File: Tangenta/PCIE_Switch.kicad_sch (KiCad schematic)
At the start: 0 parts

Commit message: PCIe current progress, hierarchy
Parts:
- added C1: 10uF, Capacitor_SMD:C_0402_1005Metric, symbol Device:C_Small
- added U15: PI7C9X2G404SLBFDEX, PCIE_Switch:PCIE_Switch, symbol PCIE_Switch:PI7C9X2G404SLBFDEX
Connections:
- new net 3V3: C1.1
- new net 3V3_STANDBY: C1.2
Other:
- note added: "Used for test purposes only!!!"

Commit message: PCIe current progress.
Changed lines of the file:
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@@
+    (stroke (width 0) (type default))
+  )
+  (wire (pts (xy 56.515 29.21) (xy 33.655 29.21))
     (stroke (width 0) (type default))
   )
@@
     (stroke (width 0) (type default))
   )
-  (wire (pts (xy 56.515 24.13) (xy 33.655 24.13))
+  (wire (pts (xy 56.515 19.05) (xy 33.655 19.05))
     (stroke (width 0) (type default))
   )
-  (wire (pts (xy 56.515 29.21) (xy 33.655 29.21))
+  (wire (pts (xy 56.515 24.13) (xy 33.655 24.13))
     (stroke (width 0) (type default))
   )
@@
   (text "Used for test purposes only!!!" (at 251.4601 72.3901 0)
     (effects (font (size 3 3)) (justify left bottom))
+  )
+  (label "1V0SB" (at 56.515 29.21 180) (fields_autoplaced)
+    (effects (font (size 1.27 1.27)) (justify right bottom))
   )
   (label "3V3" (at 280.6701 95.2501 0) (fields_autoplaced)
@@
     (effects (font (size 1.27 1.27)) (justify left bottom))
   )
-  (label "3V3" (at 56.515 29.21 180) (fields_autoplaced)
+  (label "3V3" (at 56.515 24.13 180) (fields_autoplaced)
     (effects (font (size 1.27 1.27)) (justify right bottom))
   )
@@
     (effects (font (size 1.27 1.27)) (justify right bottom))
   )
-  (label "3V3SB" (at 56.515 24.13 180) (fields_autoplaced)
+  (label "3V3SB" (at 56.515 19.05 180) (fields_autoplaced)
     (effects (font (size 1.27 1.27)) (justify right bottom))
   )
@@
     (effects (font (size 1.27 1.27)) (justify right))
   )
+  (hierarchical_label "1V0_STANDBY" (shape input) (at 33.655 29.21 180) (fields_autoplaced)
+    (effects (font (size 1.27 1.27)) (justify right))
+  )
   (hierarchical_label "PCIE_SW_SMBCLK" (shape input) (at 33.655 81.915 180) (fields_autoplaced)
     (effects (font (size 1.27 1.27)) (justify right))
@@
     (effects (font (size 1.27 1.27)) (justify right))
   )
-  (hierarchical_label "3V3_STANDBY" (shape input) (at 33.655 24.13 180) (fields_autoplaced)
+  (hierarchical_label "3V3_STANDBY" (shape input) (at 33.655 19.05 180) (fields_autoplaced)
     (effects (font (size 1.27 1.27)) (justify right))
   )
@@
     (effects (font (size 1.27 1.27)) (justify right))
   )
-  (hierarchical_label "3V3" (shape input) (at 33.655 29.21 180) (fields_autoplaced)
+  (hierarchical_label "3V3" (shape input) (at 33.655 24.13 180) (fields_autoplaced)
     (effects (font (size 1.27 1.27)) (justify right))
   )

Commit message: PCIe EEPROM
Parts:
- added C1: 10uF, Capacitor_SMD:C_0402_1005Metric, symbol Device:C_Small
- added C1: 100nF, Capacitor_SMD:C_0402_1005Metric, symbol Device:C_Small
- added R2 (x2): 5.1k, Resistor_SMD:R_0402_1005Metric, symbol Device:R_Small_US
- added U17: M24C04-RMN6TP, M24C04-RMN6TP:M24C04-RMN6TP, symbol M24C04-RMN6TP:M24C04-RMN6TP
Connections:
- net 3V3: now also C1.2, C1.2, R2.2, R2.2, U17.8 (VCC); no longer C1.1
- net 3V3_STANDBY: no longer C1.2
- net GNDREF: now also C1.1, C1.1, U17.2 (E1), U17.3 (E2), U17.4 (VSS), U17.7 (WC#)
- new net EE_I2C_SCL: R2.1, U17.6 (SCL)
- new net EE_I2C_SDA: R2.1, U17.5 (SDA)
- no-connect marks 0 -> 1
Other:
- note added: "EEPROM"
- note removed: "Used for test purposes only!!!"

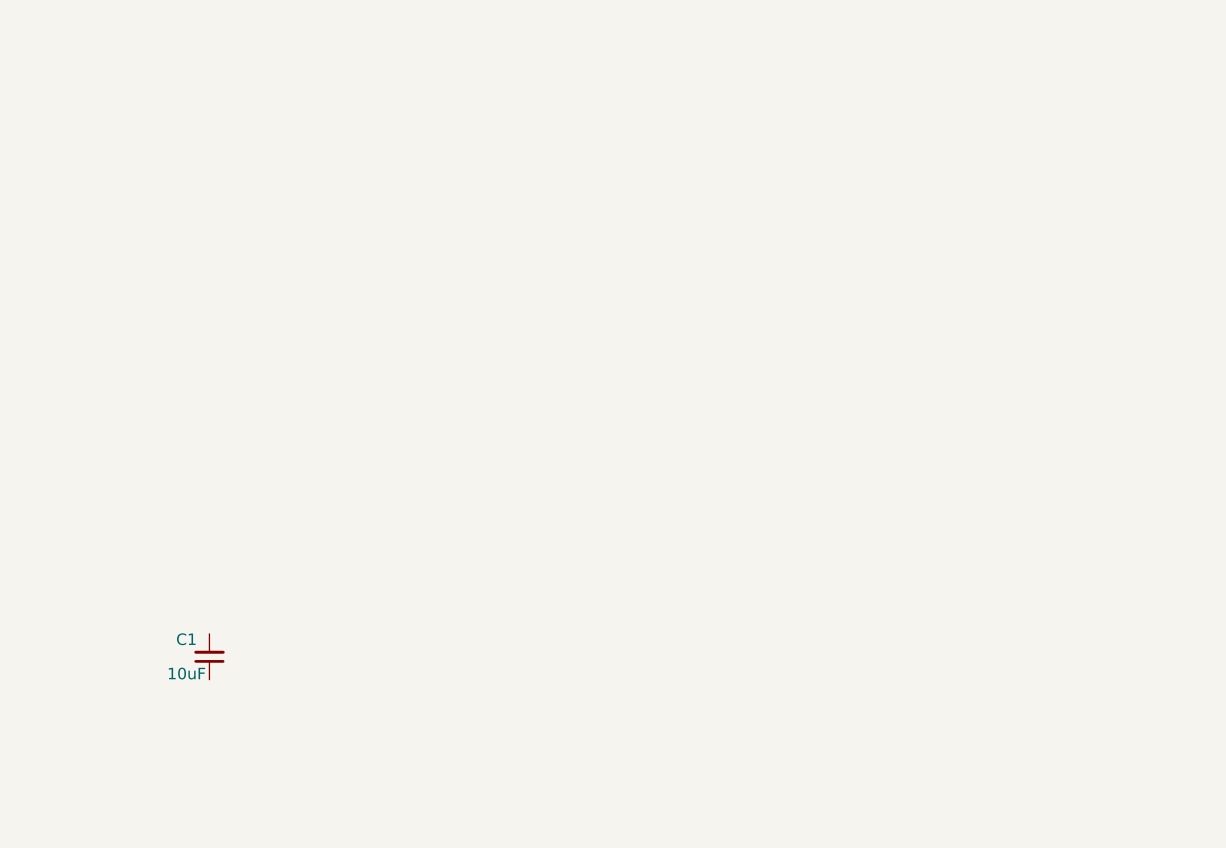
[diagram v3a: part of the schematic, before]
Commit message: PCIe 3.3V decaps.
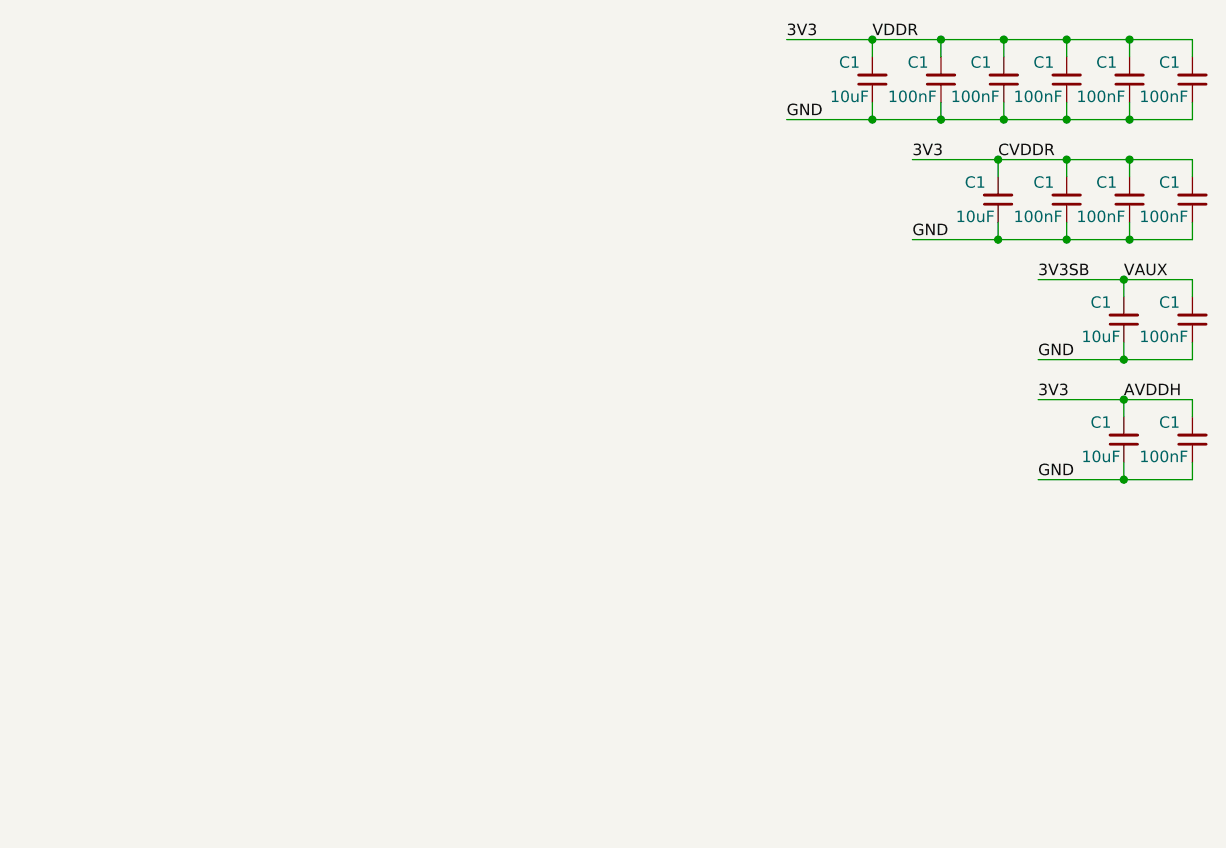
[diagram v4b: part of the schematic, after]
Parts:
- added C1 (x3): 10uF, Capacitor_SMD:C_0402_1005Metric, symbol Device:C_Small
- added C1 (x10): 100nF, Capacitor_SMD:C_0402_1005Metric, symbol Device:C_Small
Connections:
- net 3V3: now also C1.2, C1.2, C1.2, C1.2, C1.2, C1.2, C1.2, C1.2, C1.2, C1.2, C1.2, C1.2
- net 3V3_STANDBY: now also C1.2, C1.2
- net GNDREF: now also C1.1, C1.1, C1.1, C1.1, C1.1, C1.1, C1.1, C1.1, C1.1, C1.1, C1.1, C1.1, C1.1, C1.1
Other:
- moved on the sheet: C1

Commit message: ...
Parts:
- added C1 (x16): 100nF, Capacitor_SMD:C_0402_1005Metric, symbol Device:C_Small
- added C1 (x3): 10uF, Capacitor_SMD:C_0402_1005Metric, symbol Device:C_Small
- added R2: 1.43k 1%, Resistor_SMD:R_0402_1005Metric, symbol Device:R_Small_US
- added R2: 475R 1%, Resistor_SMD:R_0402_1005Metric, symbol Device:R_Small_US
- added R2: 5.1k, Resistor_SMD:R_0402_1005Metric, symbol Device:R_Small_US
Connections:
- net 1V0: now also C1.2, C1.2, C1.2, C1.2, C1.2, C1.2, C1.2, C1.2, C1.2, C1.2, C1.2, C1.2, C1.2, C1.2, C1.2, C1.2
- net 1V0_STANDBY: now also C1.2, C1.2, C1.2
- net 3V3: now also R2.2
- net GNDREF: now also C1.1, C1.1, C1.1, C1.1, C1.1, C1.1, C1.1, C1.1, C1.1, C1.1, C1.1, C1.1, C1.1, C1.1, C1.1, C1.1, C1.1, C1.1, C1.1, R2.1
- new net IREF: R2.2
- new net REXT: R2.2
- new net REXT_GND: R2.1
- new net TEST2: R2.1
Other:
- moved on the sheet: C1

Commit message: Fixing the PCIe switch symbol and grid alignment.
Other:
- moved on the sheet: C1, R2, U15, U17

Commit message: PCIe schematic continued...
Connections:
- net 1V0: now also U15.3 (VDDC)
- net 3V3: now also U15.1 (VDDR), U15.8 (VDDR)
- net GNDREF: now also U15.2 (VSS), U15.4 (VSS)
- net DWNRST1_L: now reaches U15.5 (DWNRST_L[1])
- net DWNRST2_L: now reaches U15.6 (DWNRST_L[2])
- net DWNRST3_L: now reaches U15.7 (DWNRST_L[3])
- net TEST1: now reaches U15.9 (TEST1)
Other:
- note removed: "EEPROM"

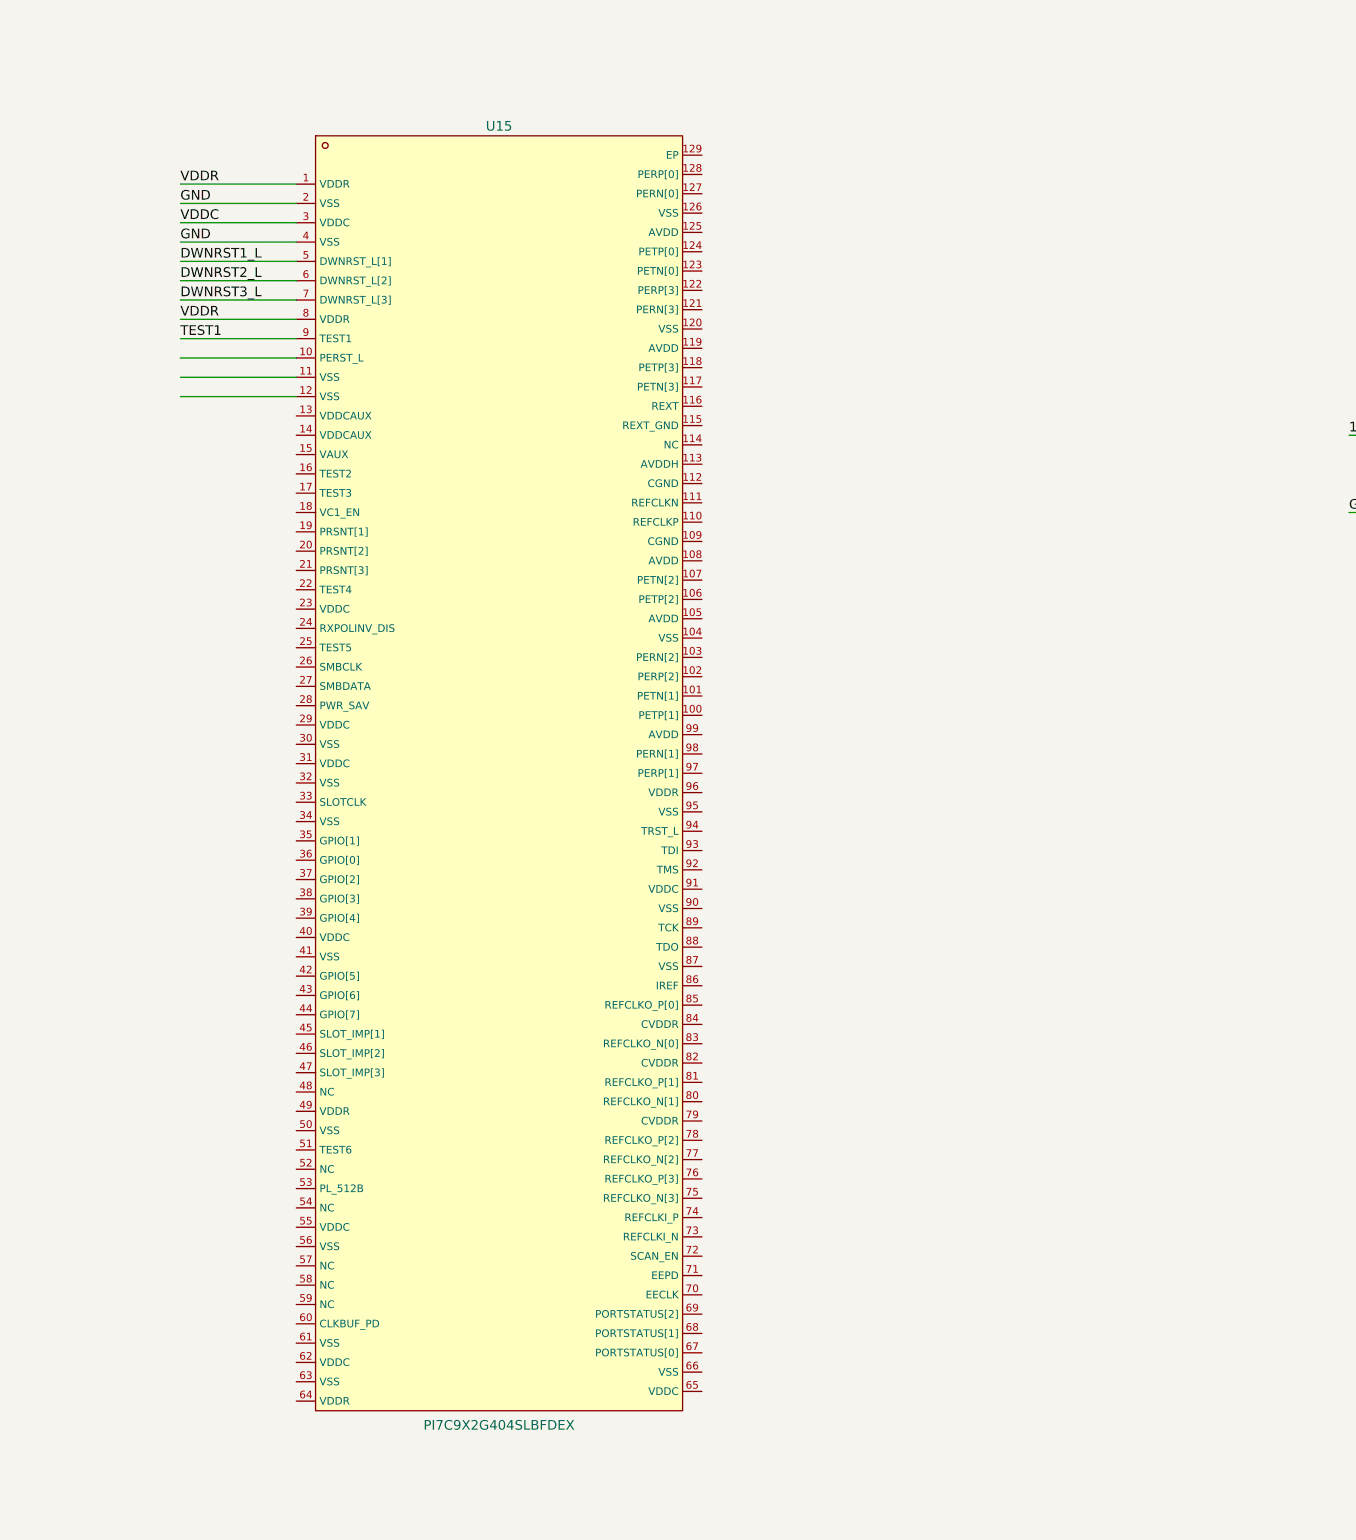
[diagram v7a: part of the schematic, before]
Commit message: PCIe switch schematic, continued...
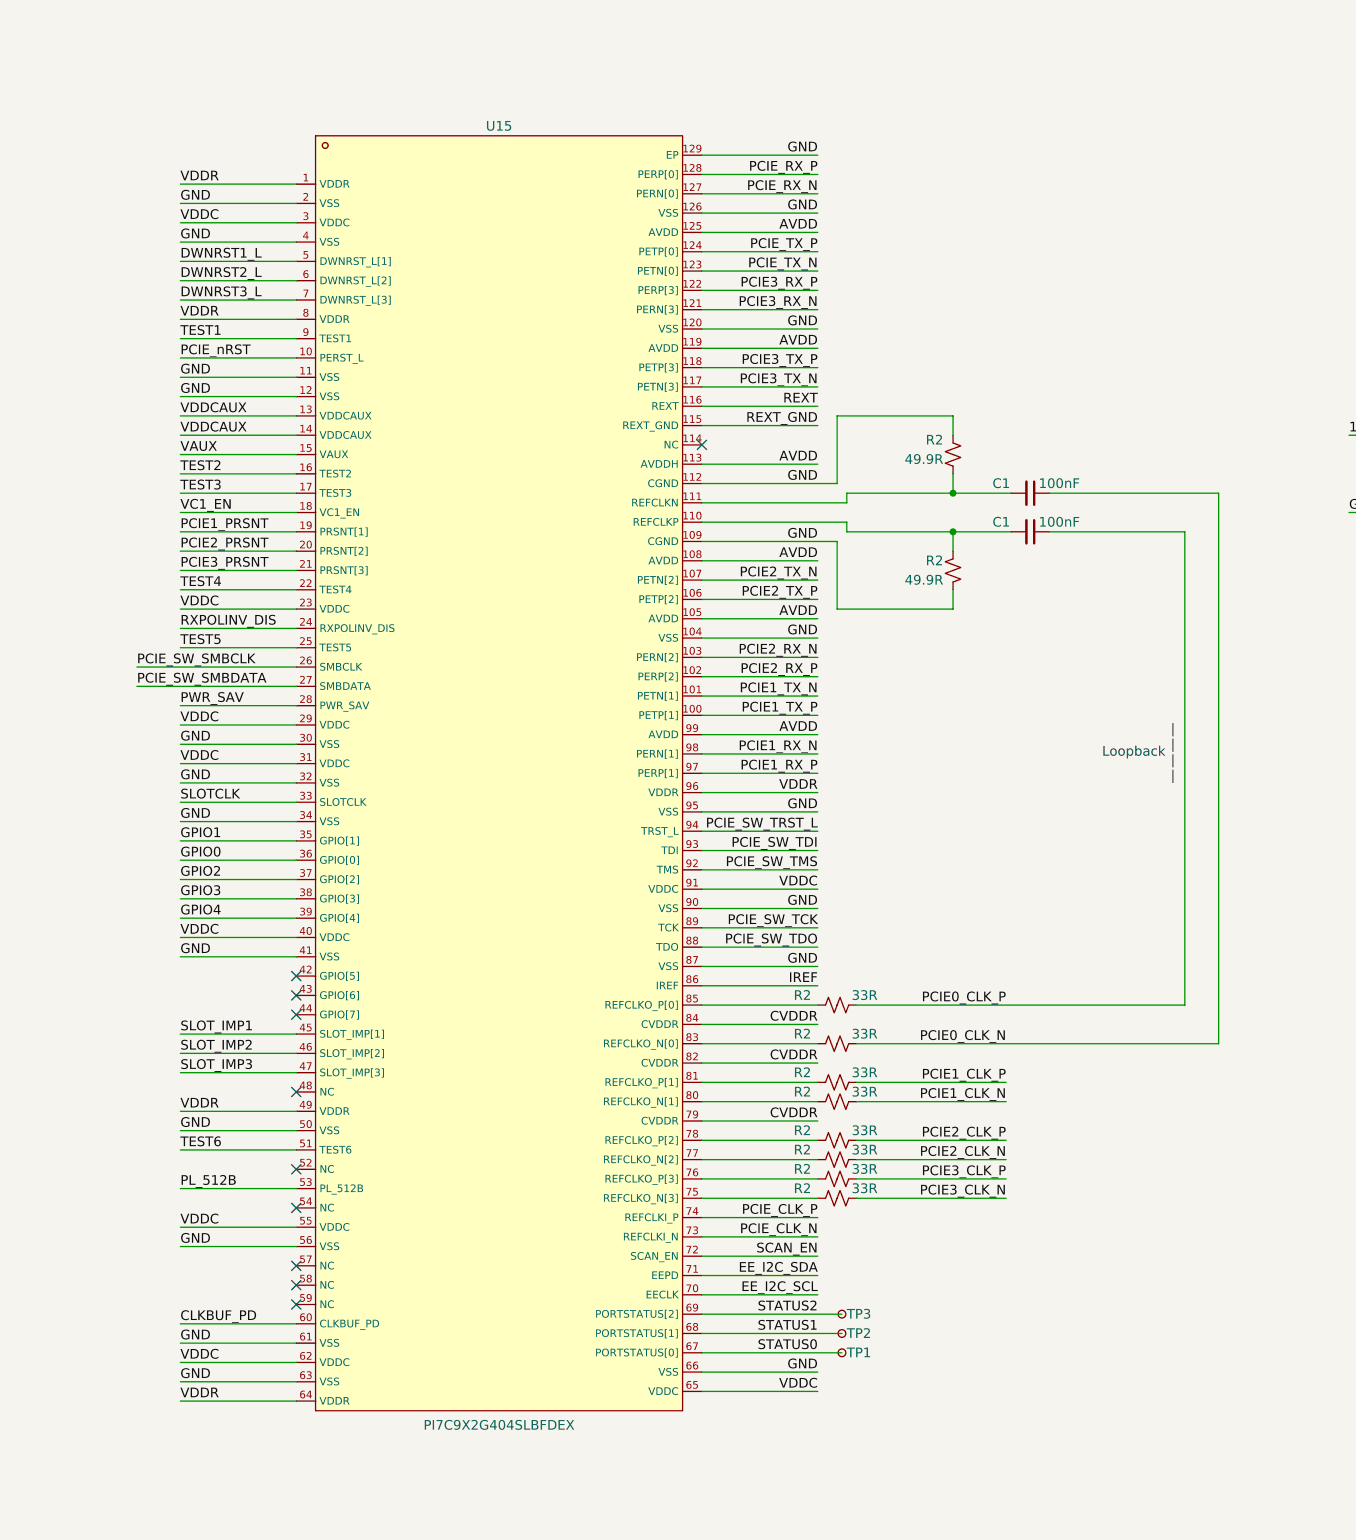
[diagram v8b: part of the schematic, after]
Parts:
- added C1 (x2): 100nF, Capacitor_SMD:C_0402_1005Metric, symbol Device:C_Small
- added R2 (x8): 33R, Resistor_SMD:R_0402_1005Metric, symbol Device:R_Small_US
- added R2 (x2): 49.9R, Resistor_SMD:R_0402_1005Metric, symbol Device:R_Small_US
- added TP1, TP2, TP3: TestPoint_Small, TestPoint:TestPoint_Pad_1.0x1.0mm, symbol Connector:TestPoint_Small
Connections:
- net 1V0: now also U15.105 (AVDD), U15.108 (AVDD), U15.113 (AVDDH), U15.119 (AVDD), U15.125 (AVDD), U15.23 (VDDC), U15.29 (VDDC), U15.31 (VDDC), U15.40 (VDDC), U15.55 (VDDC), U15.62 (VDDC), U15.65 (VDDC), U15.91 (VDDC), U15.99 (AVDD)
- net 1V0_STANDBY: now also U15.13 (VDDCAUX), U15.14 (VDDCAUX)
- net 3V3: now also U15.49 (VDDR), U15.64 (VDDR), U15.79 (CVDDR), U15.82 (CVDDR), U15.84 (CVDDR), U15.96 (VDDR)
- net 3V3_STANDBY: now also U15.15 (VAUX)
- net EE_I2C_SCL: now also U15.70 (EECLK)
- net EE_I2C_SDA: now also U15.71 (EEPD)
- net GNDREF: now also U15.104 (VSS), U15.109 (CGND), U15.11 (VSS), U15.112 (CGND), U15.12 (VSS), U15.120 (VSS), U15.126 (VSS), U15.129 (EP), U15.30 (VSS), U15.32 (VSS), U15.34 (VSS), U15.41 (VSS), U15.50 (VSS), U15.56 (VSS), U15.61 (VSS), U15.63 (VSS), U15.66 (VSS), U15.87 (VSS), U15.90 (VSS), U15.95 (VSS), R2.2, R2.2
- net IREF: now also U15.86 (IREF)
- net PCIE1_CLK_N: now also R2.1
- net PCIE1_CLK_P: now also R2.1
- net PCIE1_PRSNT: now also U15.19 (PRSNT[1])
- net PCIE1_RX_N: now also U15.98 (PERN[1])
- net PCIE1_RX_P: now also U15.97 (PERP[1])
- net PCIE1_TX_N: now also U15.101 (PETN[1])
- net PCIE1_TX_P: now also U15.100 (PETP[1])
- net PCIE2_CLK_N: now also R2.1
- net PCIE2_CLK_P: now also R2.1
- net PCIE2_PRSNT: now also U15.20 (PRSNT[2])
- net PCIE2_RX_N: now also U15.103 (PERN[2])
- net PCIE2_RX_P: now also U15.102 (PERP[2])
- net PCIE2_TX_N: now also U15.107 (PETN[2])
- net PCIE2_TX_P: now also U15.106 (PETP[2])
- net PCIE3_CLK_N: now also R2.1
- net PCIE3_CLK_P: now also R2.1
- net PCIE3_PRSNT: now also U15.21 (PRSNT[3])
- net PCIE3_RX_N: now also U15.121 (PERN[3])
- net PCIE3_RX_P: now also U15.122 (PERP[3])
- net PCIE3_TX_N: now also U15.117 (PETN[3])
- net PCIE3_TX_P: now also U15.118 (PETP[3])
- net PCIE_CLK_N: now also U15.73 (REFCLKI_N)
- net PCIE_CLK_P: now also U15.74 (REFCLKI_P)
- net PCIE_RX_N: now also U15.127 (PERN[0])
- net PCIE_RX_P: now also U15.128 (PERP[0])
- net PCIE_SW_SMBCLK: now also U15.26 (SMBCLK)
- net PCIE_SW_SMBDATA: now also U15.27 (SMBDATA)
- net PCIE_SW_TCK: now also U15.89 (TCK)
- net PCIE_SW_TDI: now also U15.93 (TDI)
- net PCIE_SW_TDO: now also U15.88 (TDO)
- net PCIE_SW_TMS: now also U15.92 (TMS)
- net PCIE_SW_TRST_L: now also U15.94 (TRST_L)
- net PCIE_TX_N: now also U15.123 (PETN[0])
- net PCIE_TX_P: now also U15.124 (PETP[0])
- net PCIE_nRST: now also U15.10 (PERST_L)
- net REXT: now also U15.116 (REXT)
- net REXT_GND: now also U15.115 (REXT_GND)
- net TEST2: now also U15.16 (TEST2)
- net at U15.110 (REFCLKP): now also C1.2, R2.1
- net at U15.111 (REFCLKN): now also C1.2, R2.1
- net TEST3: now reaches U15.17 (TEST3)
- net VC1_EN: now reaches U15.18 (VC1_EN)
- net TEST4: now reaches U15.22 (TEST4)
- net RXPOLINV_DIS: now reaches U15.24 (RXPOLINV_DIS)
- net TEST5: now reaches U15.25 (TEST5)
- net PWR_SAV: now reaches U15.28 (PWR_SAV)
- net SLOTCLK: now reaches U15.33 (SLOTCLK)
- net GPIO1: now reaches U15.35 (GPIO[1])
- net GPIO0: now reaches U15.36 (GPIO[0])
- net GPIO2: now reaches U15.37 (GPIO[2])
- net GPIO3: now reaches U15.38 (GPIO[3])
- net GPIO4: now reaches U15.39 (GPIO[4])
- net SLOT_IMP1: now reaches U15.45 (SLOT_IMP[1])
- net SLOT_IMP2: now reaches U15.46 (SLOT_IMP[2])
- net SLOT_IMP3: now reaches U15.47 (SLOT_IMP[3])
- net TEST6: now reaches U15.51 (TEST6)
- net PL_512B: now reaches U15.53 (PL_512B)
- net CLKBUF_PD: now reaches U15.60 (CLKBUF_PD)
- net STATUS0: now reaches U15.67 (PORTSTATUS[0])
- net STATUS0: now also TP1.1
- net STATUS1: now reaches U15.68 (PORTSTATUS[1])
- net STATUS1: now also TP2.1
- net STATUS2: now reaches U15.69 (PORTSTATUS[2])
- net STATUS2: now also TP3.1
- net SCAN_EN: now reaches U15.72 (SCAN_EN)
- net at U15.75 (REFCLKO_N[3]): now also R2.2
- net at U15.76 (REFCLKO_P[3]): now also R2.2
- net at U15.77 (REFCLKO_N[2]): now also R2.2
- net at U15.78 (REFCLKO_P[2]): now also R2.2
- net at U15.80 (REFCLKO_N[1]): now also R2.2
- net at U15.81 (REFCLKO_P[1]): now also R2.2
- net at U15.83 (REFCLKO_N[0]): now also R2.2
- net at U15.85 (REFCLKO_P[0]): now also R2.2
- new net PCIE0_CLK_N: C1.1, R2.1
- new net PCIE0_CLK_P: C1.1, R2.1
- no-connect marks 1 -> 11
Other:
- note added: "Loopback"
- note added: "| | | |"
